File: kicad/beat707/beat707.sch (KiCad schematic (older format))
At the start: 47 parts, among them J1 footswitch, J2 click-out, J3 MIDI-in, J4 MIDI-out, J5 USB_B, J6 free IO, J7 ISP, SW1 Rotary_Encoder_Switch, SW2 SW_Push, SW3 SW_Push, SW4 SW_Push, U1 6N138, U2 74HC14, U5 ATmega328-PU, Y1 20 MHz

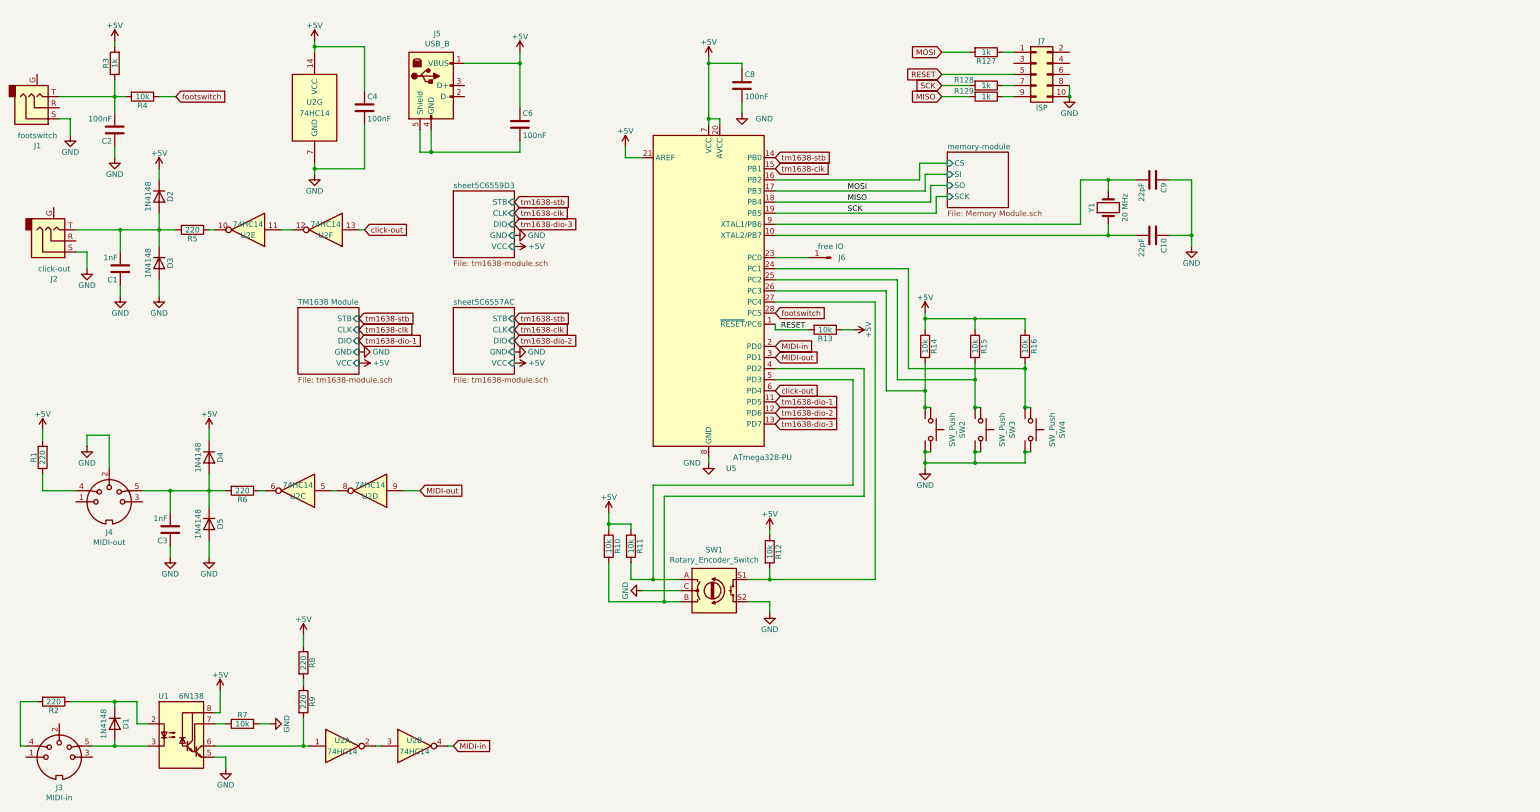
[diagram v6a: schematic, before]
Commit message: brain board added, bufixes and final board synchronized with schematic
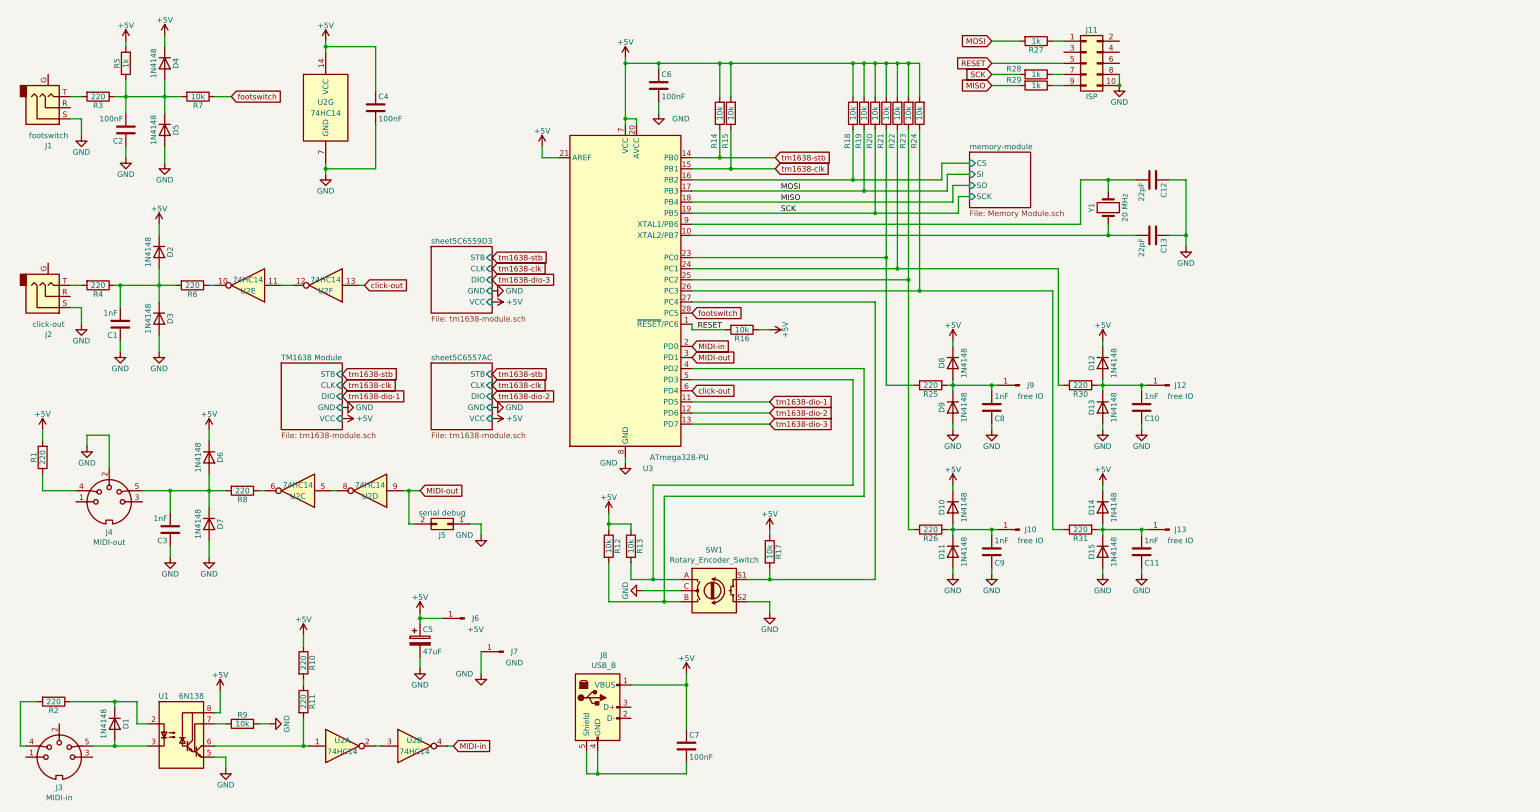
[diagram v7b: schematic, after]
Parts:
- removed R16: 10k, Resistor_THT:R_Axial_DIN0207_L6.3mm_D2.5mm_P7.62mm_Horizontal, symbol Device:R
- removed SW2, SW3, SW4: SW_Push, beat707:B3F-through-hole, symbol switch:SW_Push
- added C10, C11, C8, C9: 1nF, Capacitor_THT:C_Disc_D8.0mm_W5.0mm_P7.50mm, symbol Device:C
- added C5: 47uF, Capacitor_THT:CP_Radial_D6.3mm_P2.50mm, symbol Device:CP
- added D10, D11, D12, D13, D14, D15, D4, D5, D8, D9: 1N4148, Diode_THT:D_DO-35_SOD27_P7.62mm_Horizontal, symbol Diode:1N4148
- added J10, J12, J13: free IO, Connector_PinHeader_2.54mm:PinHeader_1x01_P2.54mm_Vertical, symbol Connector:Conn_01x01_Male
- added J5: serial debug, Connector_PinHeader_2.54mm:PinHeader_2x01_P2.54mm_Vertical, symbol Connector_Generic:Conn_02x01
- added J6: +5V, Connector_PinHeader_2.54mm:PinHeader_1x01_P2.54mm_Vertical, symbol Connector:Conn_01x01_Male
- added J7: GND, Connector_PinHeader_2.54mm:PinHeader_1x01_P2.54mm_Vertical, symbol Connector:Conn_01x01_Male
- added R18, R19, R20, R21, R22, R23, R24: 10k, Resistor_THT:R_Axial_DIN0207_L6.3mm_D2.5mm_P10.16mm_Horizontal, symbol Device:R
- added R25, R26, R3, R30, R31, R4: 220, Resistor_THT:R_Axial_DIN0207_L6.3mm_D2.5mm_P10.16mm_Horizontal, symbol Device:R
- R1, R14, R15, R2: footprint Resistor_THT:R_Axial_DIN0207_L6.3mm_D2.5mm_P7.62mm_Horizontal -> Resistor_THT:R_Axial_DIN0207_L6.3mm_D2.5mm_P10.16mm_Horizontal
- R10: renamed from R8; footprint Resistor_THT:R_Axial_DIN0207_L6.3mm_D2.5mm_P7.62mm_Horizontal -> Resistor_THT:R_Axial_DIN0207_L6.3mm_D2.5mm_P10.16mm_Horizontal
- R11: renamed from R9; footprint Resistor_THT:R_Axial_DIN0207_L6.3mm_D2.5mm_P7.62mm_Horizontal -> Resistor_THT:R_Axial_DIN0207_L6.3mm_D2.5mm_P10.16mm_Horizontal
- R12: renamed from R10; footprint Resistor_THT:R_Axial_DIN0207_L6.3mm_D2.5mm_P7.62mm_Horizontal -> Resistor_THT:R_Axial_DIN0207_L6.3mm_D2.5mm_P10.16mm_Horizontal
- R13: renamed from R11; footprint Resistor_THT:R_Axial_DIN0207_L6.3mm_D2.5mm_P7.62mm_Horizontal -> Resistor_THT:R_Axial_DIN0207_L6.3mm_D2.5mm_P10.16mm_Horizontal
- R16: renamed from R13; footprint Resistor_THT:R_Axial_DIN0207_L6.3mm_D2.5mm_P7.62mm_Horizontal -> Resistor_THT:R_Axial_DIN0207_L6.3mm_D2.5mm_P10.16mm_Horizontal
- R17: renamed from R12; footprint Resistor_THT:R_Axial_DIN0207_L6.3mm_D2.5mm_P7.62mm_Horizontal -> Resistor_THT:R_Axial_DIN0207_L6.3mm_D2.5mm_P10.16mm_Horizontal
- R27: renamed from R127; footprint Resistor_THT:R_Axial_DIN0207_L6.3mm_D2.5mm_P7.62mm_Horizontal -> Resistor_THT:R_Axial_DIN0207_L6.3mm_D2.5mm_P10.16mm_Horizontal
- R28: renamed from R128; footprint Resistor_THT:R_Axial_DIN0207_L6.3mm_D2.5mm_P7.62mm_Horizontal -> Resistor_THT:R_Axial_DIN0207_L6.3mm_D2.5mm_P10.16mm_Horizontal
- R29: renamed from R129; footprint Resistor_THT:R_Axial_DIN0207_L6.3mm_D2.5mm_P7.62mm_Horizontal -> Resistor_THT:R_Axial_DIN0207_L6.3mm_D2.5mm_P10.16mm_Horizontal
- R5: renamed from R3; footprint Resistor_THT:R_Axial_DIN0207_L6.3mm_D2.5mm_P7.62mm_Horizontal -> Resistor_THT:R_Axial_DIN0207_L6.3mm_D2.5mm_P10.16mm_Horizontal
- R6: renamed from R5; footprint Resistor_THT:R_Axial_DIN0207_L6.3mm_D2.5mm_P7.62mm_Horizontal -> Resistor_THT:R_Axial_DIN0207_L6.3mm_D2.5mm_P10.16mm_Horizontal
- R7: renamed from R4; footprint Resistor_THT:R_Axial_DIN0207_L6.3mm_D2.5mm_P7.62mm_Horizontal -> Resistor_THT:R_Axial_DIN0207_L6.3mm_D2.5mm_P10.16mm_Horizontal
- R8: renamed from R6; footprint Resistor_THT:R_Axial_DIN0207_L6.3mm_D2.5mm_P7.62mm_Horizontal -> Resistor_THT:R_Axial_DIN0207_L6.3mm_D2.5mm_P10.16mm_Horizontal
- R9: renamed from R7; footprint Resistor_THT:R_Axial_DIN0207_L6.3mm_D2.5mm_P7.62mm_Horizontal -> Resistor_THT:R_Axial_DIN0207_L6.3mm_D2.5mm_P10.16mm_Horizontal
- renumbered C9 to C12, C10 to C13, C8 to C6, C6 to C7, D4 to D6, D5 to D7, J7 to J11, J5 to J8, J6 to J9, U5 to U3
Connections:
- net +5V: now also R14.2, R15.2, C5.1, D10.1 (K), D12.1 (K), D14.1 (K), D4.1 (K), D8.1 (K), J6.1 (Pin_1), R18.2, R19.2, R20.2, R21.2, R22.2, R23.2, R24.2; no longer R14.1, R15.1
- net GND: now also C10.1, C11.1, C5.2, C8.1, C9.1, D11.2 (A), D13.2 (A), D15.2 (A), D5.2 (A), D9.2 (A), J5.1 (Pin_1), J7.1 (Pin_1)
- net MIDI-out: now also J5.2 (Pin_2)
- net MOSI: now also R19.1
- net SCK: now also R20.1
- net memory-module/CS: now also R18.1
- net tm1638-clk: now also R15.1
- net tm1638-stb: now also R14.1
- net at U3.23 (PC0): now also R21.1, R25.1; no longer J9.1 (Pin_1)
- net at U3.24 (PC1): now also R22.1, R30.1
- net at U3.25 (PC2): now also R23.1, R26.1; no longer R15.2
- net at U3.26 (PC3): now also R24.1, R31.1; no longer R14.2
- net at C1.2, D2.2 (A), D3.1 (K)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: now also R4.1; no longer J2.T
- net at C2.2, R5.1, R7.2: now also D4.2 (A), D5.1 (K), R3.1; no longer J1.T
- new net: J2.T, R4.2
- new net: J1.T, R3.2
- new net: C8.2, D8.2 (A), D9.1 (K), J9.1 (Pin_1), R25.2
- new net: C10.2, D12.2 (A), D13.1 (K), J12.1 (Pin_1), R30.2
- new net: C9.2, D10.2 (A), D11.1 (K), J10.1 (Pin_1), R26.2
- new net: C11.2, D14.2 (A), D15.1 (K), J13.1 (Pin_1), R31.2
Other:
- moved on the sheet: C1, C2, C4, C6, C7, D2, D3, J1, J11, J2, J8, J9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

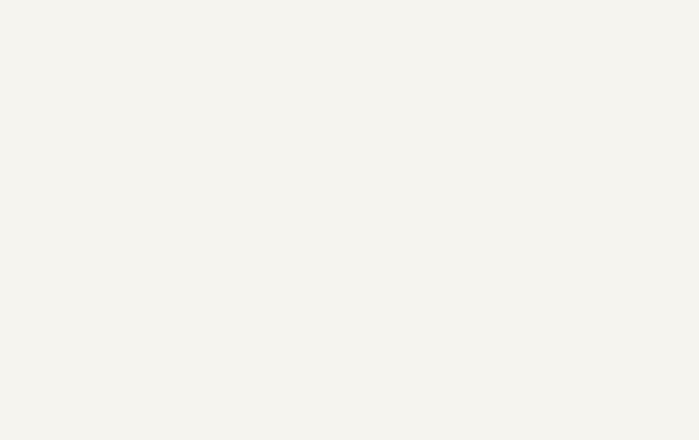
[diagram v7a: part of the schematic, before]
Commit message: mounting holes
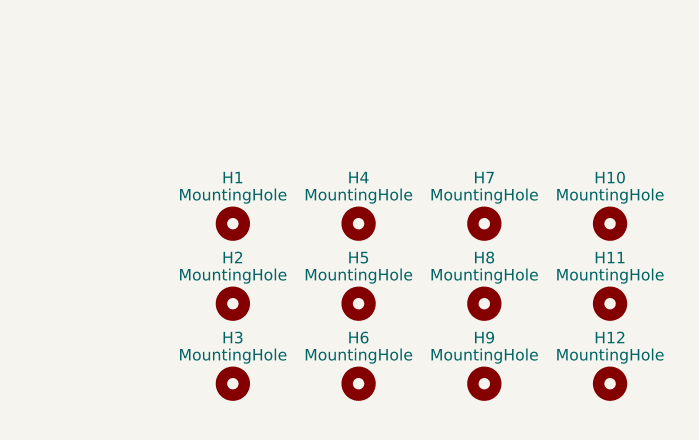
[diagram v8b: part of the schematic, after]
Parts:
- added H1, H10, H11, H12, H2, H3, H4, H5, H6, H7, H8, H9: MountingHole, MountingHole:MountingHole_3.2mm_M3, symbol Mechanical:MountingHole
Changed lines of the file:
@@
 Wire Wire Line
 	4750 6300 4750 6500
+$Comp
+L Mechanical:MountingHole H1
+U 1 1 5CCF02BE
+P 12250 6800
+F 0 "H1" H 12250 7000 50  0000 C CNN
+F 1 "MountingHole" H 12250 6925 50  0000 C CNN
+F 2 "MountingHole:MountingHole_3.2mm_M3" H 12250 6800 50  0001 C CNN
+F 3 "~" H 12250 6800 50  0001 C CNN
+	1    12250 6800
+	1    0    0    -1
+$EndComp
+$Comp
+L Mechanical:MountingHole H4
+U 1 1 5CCF149B
+P 12800 6800
+F 0 "H4" H 12800 7000 50  0000 C CNN
+F 1 "MountingHole" H 12800 6925 50  0000 C CNN
+F 2 "MountingHole:MountingHole_3.2mm_M3" H 12800 6800 50  0001 C CNN
+F 3 "~" H 12800 6800 50  0001 C CNN
+	1    12800 6800
+	1    0    0    -1
+$EndComp
+$Comp
+L Mechanical:MountingHole H7
+U 1 1 5CCF27B9
+P 13350 6800
+F 0 "H7" H 13350 7000 50  0000 C CNN
+F 1 "MountingHole" H 13350 6925 50  0000 C CNN
+F 2 "MountingHole:MountingHole_3.2mm_M3" H 13350 6800 50  0001 C CNN
+F 3 "~" H 13350 6800 50  0001 C CNN
+	1    13350 6800
+	1    0    0    -1
+$EndComp
+$Comp
+L Mechanical:MountingHole H10
+U 1 1 5CCF39C0
+P 13900 6800
+F 0 "H10" H 13900 7000 50  0000 C CNN
+F 1 "MountingHole" H 13900 6925 50  0000 C CNN
+F 2 "MountingHole:MountingHole_3.2mm_M3" H 13900 6800 50  0001 C CNN
+F 3 "~" H 13900 6800 50  0001 C CNN
+	1    13900 6800
+	1    0    0    -1
+$EndComp
+$Comp
+L Mechanical:MountingHole H2
+U 1 1 5CD0D199
+P 12250 7150
+F 0 "H2" H 12250 7350 50  0000 C CNN
+F 1 "MountingHole" H 12250 7275 50  0000 C CNN
+F 2 "MountingHole:MountingHole_3.2mm_M3" H 12250 7150 50  0001 C CNN
+F 3 "~" H 12250 7150 50  0001 C CNN
+	1    12250 7150
+	1    0    0    -1
+$EndComp
+$Comp
+L Mechanical:MountingHole H5
+U 1 1 5CD0D19F
+P 12800 7150
+F 0 "H5" H 12800 7350 50  0000 C CNN
+F 1 "MountingHole" H 12800 7275 50  0000 C CNN
+F 2 "MountingHole:MountingHole_3.2mm_M3" H 12800 7150 50  0001 C CNN
+F 3 "~" H 12800 7150 50  0001 C CNN
+	1    12800 7150
+	1    0    0    -1
+$EndComp
+$Comp
+L Mechanical:MountingHole H8
+U 1 1 5CD0D1A5
+P 13350 7150
+F 0 "H8" H 13350 7350 50  0000 C CNN
+F 1 "MountingHole" H 13350 7275 50  0000 C CNN
+F 2 "MountingHole:MountingHole_3.2mm_M3" H 13350 7150 50  0001 C CNN
+F 3 "~" H 13350 7150 50  0001 C CNN
+	1    13350 7150
+	1    0    0    -1
+$EndComp
+$Comp
+L Mechanical:MountingHole H11
+U 1 1 5CD0D1AB
+P 13900 7150
+F 0 "H11" H 13900 7350 50  0000 C CNN
+F 1 "MountingHole" H 13900 7275 50  0000 C CNN
+F 2 "MountingHole:MountingHole_3.2mm_M3" H 13900 7150 50  0001 C CNN
+F 3 "~" H 13900 7150 50  0001 C CNN
+	1    13900 7150
+	1    0    0    -1
+$EndComp
+$Comp
+L Mechanical:MountingHole H3
+U 1 1 5CD1F5E7
+P 12250 7500
+F 0 "H3" H 12250 7700 50  0000 C CNN
+F 1 "MountingHole" H 12250 7625 50  0000 C CNN
+F 2 "MountingHole:MountingHole_3.2mm_M3" H 12250 7500 50  0001 C CNN
+F 3 "~" H 12250 7500 50  0001 C CNN
+	1    12250 7500
+	1    0    0    -1
+$EndComp
+$Comp
+L Mechanical:MountingHole H6
+U 1 1 5CD1F5ED
+P 12800 7500
+F 0 "H6" H 12800 7700 50  0000 C CNN
+F 1 "MountingHole" H 12800 7625 50  0000 C CNN
+F 2 "MountingHole:MountingHole_3.2mm_M3" H 12800 7500 50  0001 C CNN
+F 3 "~" H 12800 7500 50  0001 C CNN
+	1    12800 7500
+	1    0    0    -1
+$EndComp
+$Comp
+L Mechanical:MountingHole H9
+U 1 1 5CD1F5F3
+P 13350 7500
+F 0 "H9" H 13350 7700 50  0000 C CNN
+F 1 "MountingHole" H 13350 7625 50  0000 C CNN
+F 2 "MountingHole:MountingHole_3.2mm_M3" H 13350 7500 50  0001 C CNN
+F 3 "~" H 13350 7500 50  0001 C CNN
+	1    13350 7500
+	1    0    0    -1
+$EndComp
+$Comp
+L Mechanical:MountingHole H12
+U 1 1 5CD1F5F9
+P 13900 7500
+F 0 "H12" H 13900 7700 50  0000 C CNN
+F 1 "MountingHole" H 13900 7625 50  0000 C CNN
+F 2 "MountingHole:MountingHole_3.2mm_M3" H 13900 7500 50  0001 C CNN
+F 3 "~" H 13900 7500 50  0001 C CNN
+	1    13900 7500
+	1    0    0    -1
+$EndComp
 $EndSCHEMATC
